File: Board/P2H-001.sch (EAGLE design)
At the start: 27 parts, among them IC1 LTC485N, IC2 74LS07N, IC3 74LS157N, IC4 LTC485N, IC5 TLC5941NT

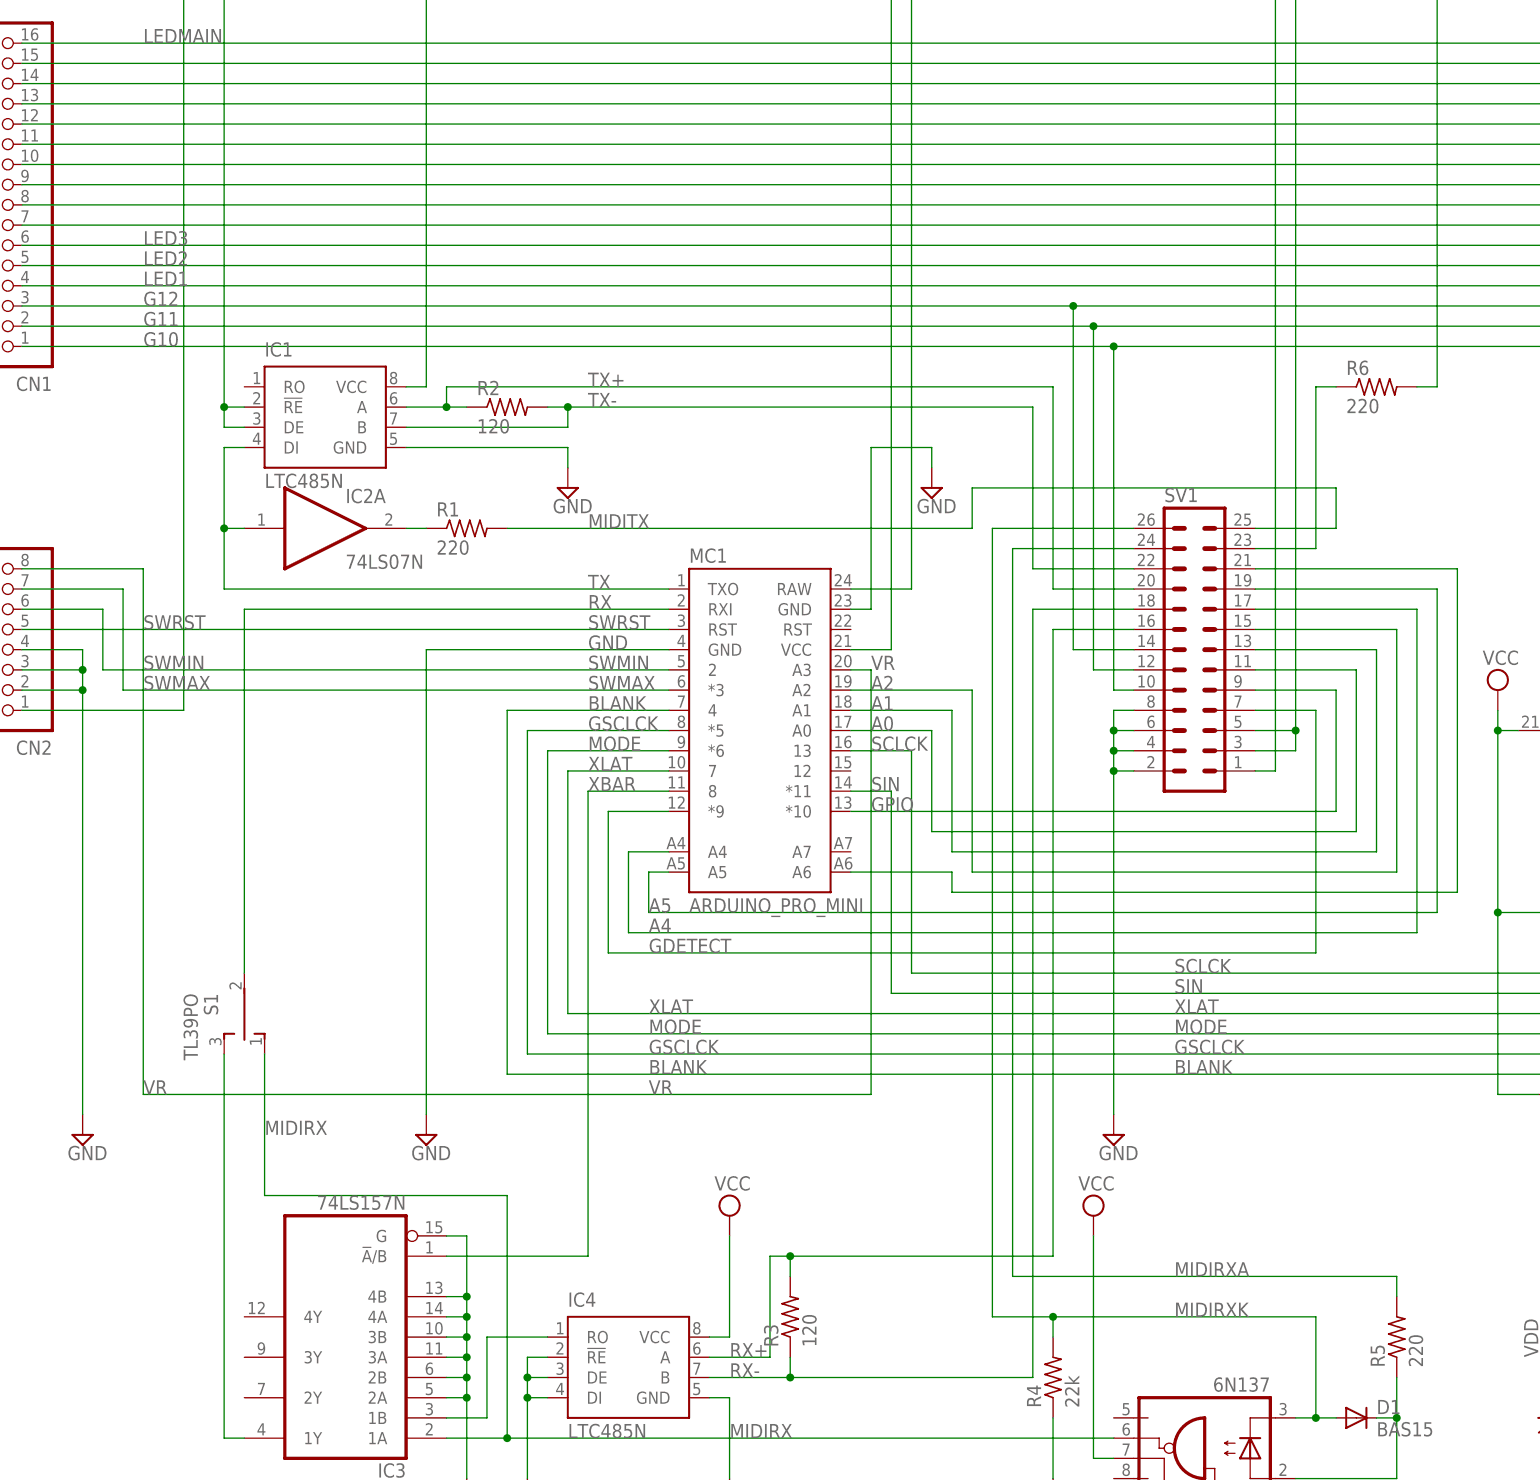
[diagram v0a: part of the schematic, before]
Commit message: Renumbered LED numbers.
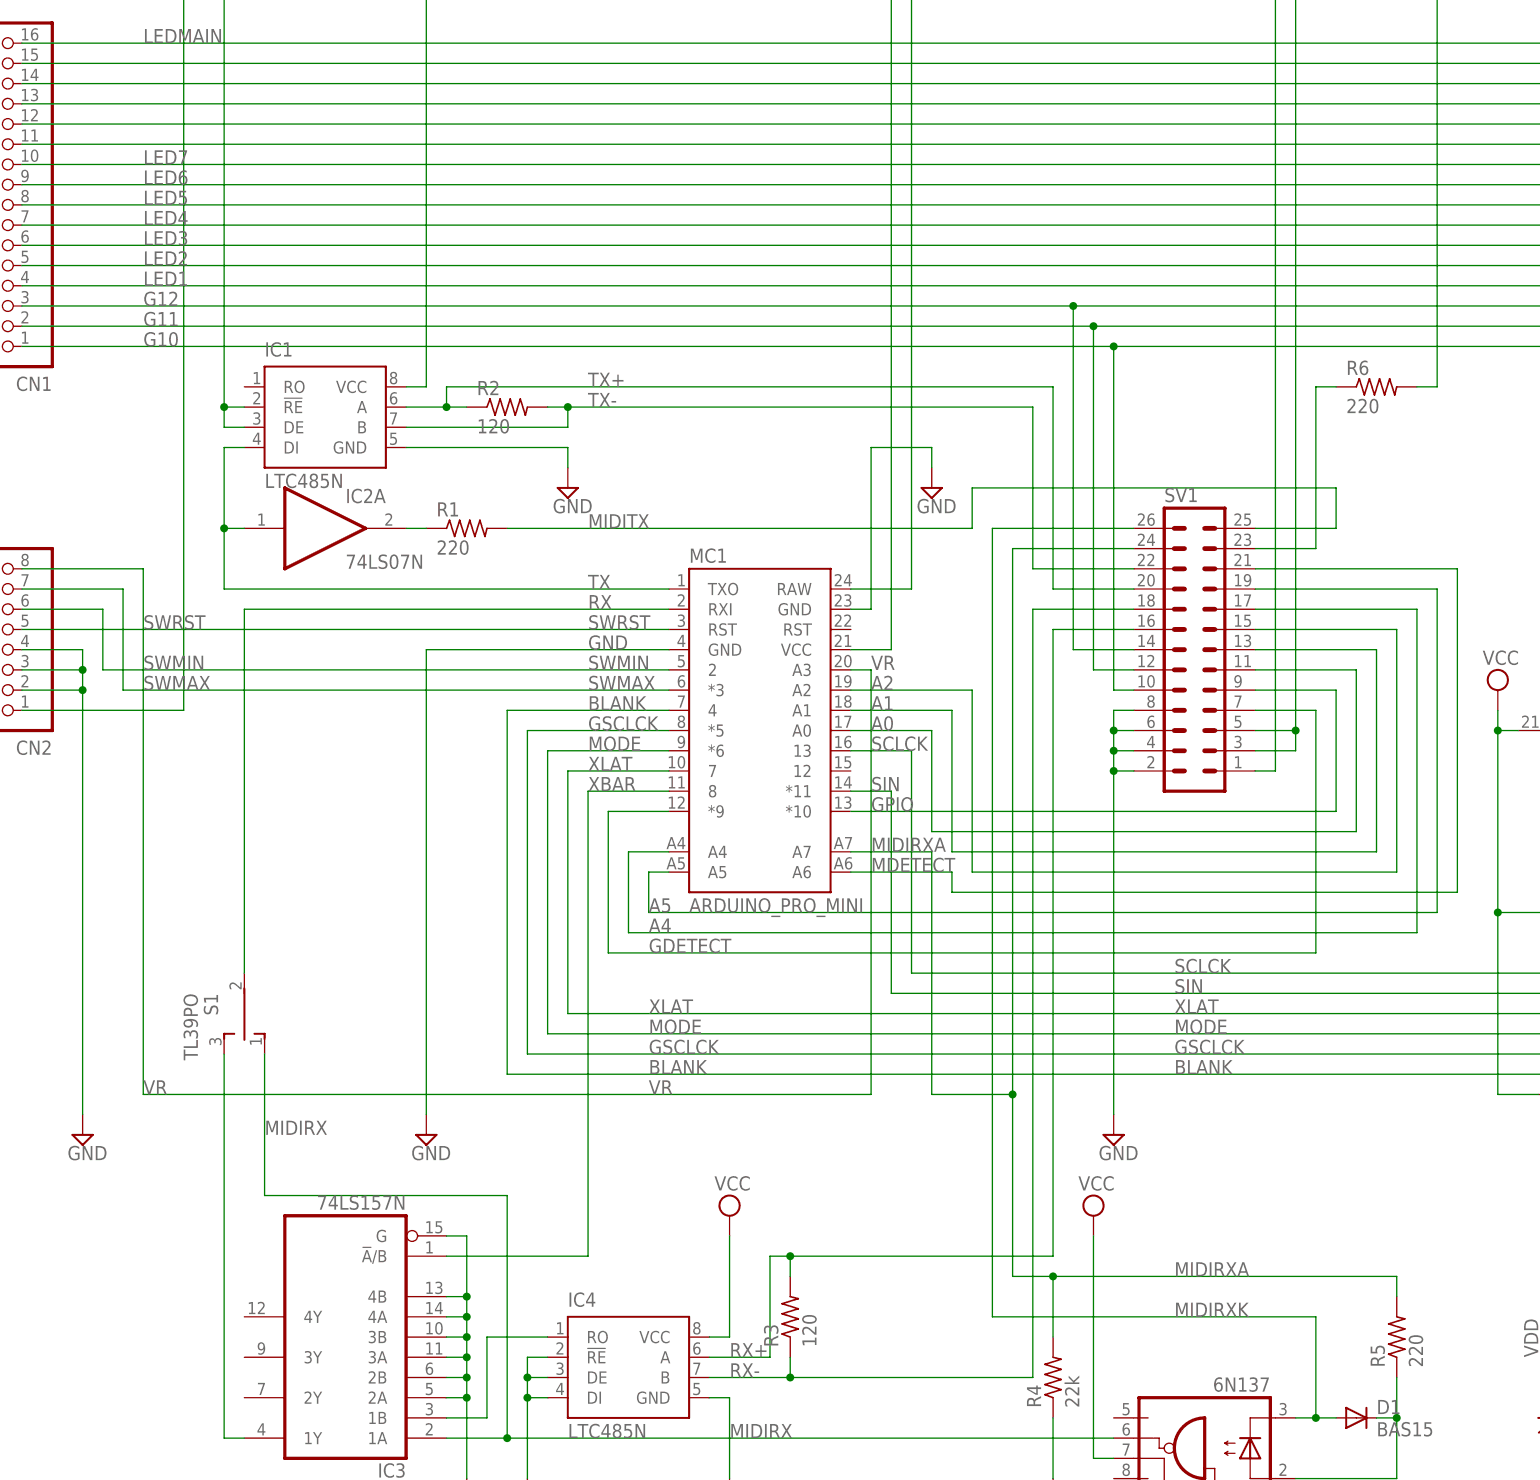
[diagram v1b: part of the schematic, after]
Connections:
- net LED3B renamed LED6
- net LED3G renamed LED5
- net LED3R renamed LED4
- net N$4 renamed MDETECT
- net N$6 renamed LED7
- net N$7 renamed LED8
- net N$8 renamed LED9
- net MIDIRXA: now also MC1.A7, R4.2
- net MIDIRXK: no longer R4.2
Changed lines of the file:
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@@
 </segment>
 </net>
-<net name="LED3R" class="0">
+<net name="LED4" class="0">
 <segment>
 <pinref part="IC5" gate="G$1" pin="OUT6"/>
@@
 <wire x1="5.08" y1="91.44" x2="215.9" y2="91.44" width="0.1524" layer="91"/>
 <pinref part="CN1" gate="G$1" pin="7"/>
-</segment>
-</net>
-<net name="LED3B" class="0">
+<label x="20.32" y="91.44" size="1.778" layer="95"/>
+</segment>
+</net>
+<net name="LED6" class="0">
 <segment>
 <pinref part="IC5" gate="G$1" pin="OUT8"/>
@@
 <wire x1="5.08" y1="96.52" x2="220.98" y2="96.52" width="0.1524" layer="91"/>
 <pinref part="CN1" gate="G$1" pin="9"/>
-</segment>
-</net>
-<net name="LED3G" class="0">
+<label x="20.32" y="96.52" size="1.778" layer="95"/>
+</segment>
+</net>
+<net name="LED5" class="0">
 <segment>
 <pinref part="IC5" gate="G$1" pin="OUT7"/>
@@
 <wire x1="5.08" y1="93.98" x2="218.44" y2="93.98" width="0.1524" layer="91"/>
 <pinref part="CN1" gate="G$1" pin="8"/>
+<label x="20.32" y="93.98" size="1.778" layer="95"/>
 </segment>
 </net>
@@
 </segment>
 </net>
-<net name="N$6" class="0">
+<net name="LED7" class="0">
 <segment>
 <pinref part="IC5" gate="G$1" pin="OUT9"/>
@@
 <wire x1="5.08" y1="99.06" x2="223.52" y2="99.06" width="0.1524" layer="91"/>
 <pinref part="CN1" gate="G$1" pin="10"/>
-</segment>
-</net>
-<net name="N$7" class="0">
+<label x="20.32" y="99.06" size="1.778" layer="95"/>
+</segment>
+</net>
+<net name="LED8" class="0">
 <segment>
 <pinref part="IC5" gate="G$1" pin="OUT10"/>
@@
 </segment>
 </net>
-<net name="N$8" class="0">
+<net name="LED9" class="0">
 <segment>
 <pinref part="IC5" gate="G$1" pin="OUT11"/>
@@
 <wire x1="167.64" y1="-58.42" x2="170.18" y2="-58.42" width="0.1524" layer="91"/>
 <wire x1="167.64" y1="-58.42" x2="167.64" y2="-45.72" width="0.1524" layer="91"/>
-<wire x1="167.64" y1="-45.72" x2="134.62" y2="-45.72" width="0.1524" layer="91"/>
+<wire x1="167.64" y1="-45.72" x2="127" y2="-45.72" width="0.1524" layer="91"/>
 <junction x="167.64" y="-58.42"/>
 <label x="149.86" y="-45.72" size="1.778" layer="95"/>
-<pinref part="R4" gate="G$1" pin="2"/>
-<wire x1="134.62" y1="-45.72" x2="134.62" y2="-48.26" width="0.1524" layer="91"/>
-<junction x="134.62" y="-45.72"/>
-<wire x1="134.62" y1="-45.72" x2="127" y2="-45.72" width="0.1524" layer="91"/>
 <wire x1="127" y1="-45.72" x2="127" y2="53.34" width="0.1524" layer="91"/>
 <pinref part="SV1" gate="1" pin="26"/>
@@
 </segment>
 </net>
-<net name="N$4" class="0">
+<net name="MDETECT" class="0">
 <segment>
 <pinref part="SV1" gate="1" pin="21"/>
@@
 <pinref part="MC1" gate="G$1" pin="A6"/>
 <wire x1="121.92" y1="10.16" x2="109.22" y2="10.16" width="0.1524" layer="91"/>
+<label x="111.76" y="10.16" size="1.778" layer="95"/>
 </segment>
 </net>
@@
 <pinref part="SV1" gate="1" pin="24"/>
 <wire x1="144.78" y1="50.8" x2="129.54" y2="50.8" width="0.1524" layer="91"/>
-<wire x1="129.54" y1="50.8" x2="129.54" y2="-40.64" width="0.1524" layer="91"/>
+<wire x1="129.54" y1="50.8" x2="129.54" y2="-17.78" width="0.1524" layer="91"/>
 <pinref part="R5" gate="G$1" pin="2"/>
-<wire x1="129.54" y1="-40.64" x2="177.8" y2="-40.64" width="0.1524" layer="91"/>
+<wire x1="129.54" y1="-17.78" x2="129.54" y2="-40.64" width="0.1524" layer="91"/>
+<wire x1="129.54" y1="-40.64" x2="134.62" y2="-40.64" width="0.1524" layer="91"/>
+<wire x1="134.62" y1="-40.64" x2="177.8" y2="-40.64" width="0.1524" layer="91"/>
 <wire x1="177.8" y1="-40.64" x2="177.8" y2="-43.18" width="0.1524" layer="91"/>
 <label x="149.86" y="-40.64" size="1.778" layer="95"/>
-</segment>
-</net>
+<pinref part="MC1" gate="G$1" pin="A7"/>
+<wire x1="109.22" y1="12.7" x2="119.38" y2="12.7" width="0.1524" layer="91"/>
+<wire x1="119.38" y1="12.7" x2="119.38" y2="-17.78" width="0.1524" layer="91"/>
+<wire x1="119.38" y1="-17.78" x2="129.54" y2="-17.78" width="0.1524" layer="91"/>
+<junction x="129.54" y="-17.78"/>
+<label x="111.76" y="12.7" size="1.778" layer="95"/>
+<pinref part="R4" gate="G$1" pin="2"/>
+<wire x1="134.62" y1="-40.64" x2="134.62" y2="-48.26" width="0.1524" layer="91"/>
+<junction x="134.62" y="-40.64"/>
+</segment>
+</net>

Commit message: Still updating.
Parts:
- removed SV2: (no value), con-ml:ML10
- added JP1: (no value), pinhead:PINHD-2X5
- added U$1: MAX7219DIP, SparkFun-DigitalIC:MAX7219DIP
- IC5: value TLC5941NT -> 4051N; device adafruit:TLC5941NT -> 40xx:4051N
- R7: value 4.7k -> (none)
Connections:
- removed net A4: MC1.A4, SV1.17
- removed net A5: MC1.A5, SV1.19
- removed net G10: CN1.1, IC5.OUT0, SV1.10
- removed net G11: CN1.2, IC5.OUT1, SV1.12
- removed net G12: CN1.3, IC5.OUT2, SV1.14
- removed net GDETECT: MC1.*9, SV1.7
- removed net GPIO: MC1.*10, SV1.9
- removed net GSCLCK: IC5.GSCLK, MC1.*5, SV2.7
- removed net LED1: CN1.4, IC5.OUT3
- removed net LED2: CN1.5, IC5.OUT4
- removed net LED3: CN1.6, IC5.OUT5
- removed net LED4: CN1.7, IC5.OUT6
- removed net LED5: CN1.8, IC5.OUT7
- removed net LED6: CN1.9, IC5.OUT8
- removed net LED7: CN1.10, IC5.OUT9
- removed net LED8: CN1.11, IC5.OUT10
- removed net LED9: CN1.12, IC5.OUT11
- removed net LEDMAIN: CN1.16, IC5.OUT15
- removed net MDETECT: MC1.A6, SV1.21
- removed net MODE: IC5.MODE, MC1.*6, SV2.8
- removed net N$10: IC5.SOUT, SV2.3
- removed net N$20: R6.1, SV1.23
- removed net N$37: IC5.IREF, R7.2
- removed net SIN: IC5.SIN, MC1.*11
- removed net VR: CN2.8, MC1.A3
- removed net XLAT: IC5.XLAT, MC1.7, SV2.6
- new net ADETECT: IC5A.X, MC1.A3
- new net DOUT: JP1.4, U$1.DOUT
- new net GSELECT: MC1.*10, SV1.15
- new net LA0: CN1.9, U$1.SEGDP
- new net LK0: CN1.1, U$1.DIG0
- new net LOAD: JP1.6, MC1.7, U$1.LOAD
- new net MOSI: JP1.3, MC1.*11, U$1.DIN
- new net N$12: R6.1, SV1.20
- new net N$18: CN1.3, U$1.DIG2
- new net N$19: CN1.4, U$1.DIG3
- new net N$21: R7.1, U$1.ISET
- new net N$22: CN1.2, U$1.DIG1
- new net N$25: CN1.6, U$1.DIG5
- new net N$26: CN1.7, U$1.DIG6
- new net N$27: CN1.8, U$1.DIG7
- new net N$29: CN1.10, U$1.SEGA
- new net N$30: CN1.11, U$1.SEGB
- new net N$31: CN1.12, U$1.SEGC
- new net N$32: CN1.13, U$1.SEGD
- new net N$33: CN1.14, U$1.SEGE
- new net N$34: CN1.15, U$1.SEGF
- new net N$35: CN1.16, U$1.SEGG
- new net N$6: IC5A.X3, SV1.14
- new net OUT1: MC1.*5, SV1.17
- new net OUT2: MC1.*6, SV1.19
- new net OUT3: MC1.*9, SV1.21
- new net SDA: MC1.A4, SV1.9
- new net SDL: MC1.A5, SV1.11
- new net SELECT0: IC5A.A, MC1.A6
- new net SELECT1: IC5A.B, MC1.A7
- new net VDETECT: CN2.8, IC5A.X0
- net A0: now also SV1.3; no longer SV1.11
- net A1: now also SV1.5; no longer SV1.13
- net A2: now also SV1.7; no longer SV1.15
- net BLANK: now also JP1.7, MC1.8; no longer IC5.BLANK, MC1.4, SV2.5
- net GND: now also IC5A.C, IC5A.INH, JP1.2, U$1.GND, U$1.GND2; no longer IC5.GND, SV2.10, SV2.2
- net MIDIRXA: now also SV1.16; no longer MC1.A7, R4.2, SV1.24
- net MIDIRXK: now also SV1.18; no longer SV1.26
- net MIDITX: now also SV1.22; no longer SV1.25
- net N$24: now also CN1.5, U$1.DIG4; no longer CN1.15, IC5.OUT14
- net N$3: now also IC5A.X1, SV1.13; no longer CN1.13, IC5.OUT12
- net N$5: now also IC5A.X2, R4.2, SV1.12; no longer CN1.14, IC5.OUT13
- net RX+: now also R3.1, SV1.24; no longer R3.2, SV1.16
- net RX-: now also R3.2, SV1.26; no longer R3.1, SV1.18
- net SCLCK: now also JP1.5, U$1.CLK; no longer IC5.SCLK, SV2.4
- net SWMAX: now also JP1.9
- net SWMIN: now also JP1.8
- net TX+: now also SV1.23; no longer SV1.20
- net TX-: now also SV1.25; no longer SV1.22
- net VCC: now also JP1.1, R7.2, U$1.VCC; no longer IC5.TEST, IC5.VCC, R7.1, SV2.1
- net VDD: now also JP1.10, SV1.10; no longer SV1.3, SV1.5, SV2.9
- net XBAR: now also MC1.4; no longer MC1.8
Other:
- note added: "Pineapple II Hydrogen 0.4.0 Copyright 2015 by Pineapple.cc"
- note removed: "Pineapple II Hydrogen 0.3.0 Copyright 2015 by Pineapple.cc"
- moved on the sheet: C1, C2, C3, C4, C5, C6, C7, CN1, D1, IC1, IC2A, IC2B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

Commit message: Autorouted.
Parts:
- IC1: value LTC485N -> 74LS157N; device linear-technology:LTC485N -> 74xx-us:74LS157N
- IC2: value 74LS07N -> LTC485N; device 74xx-us:74LS07N -> linear-technology:LTC485N
- IC3: value 74LS157N -> 4051N; device 74xx-us:74LS157N -> 40xx:4051N
- IC4: value LTC485N -> 74LS07N; device linear-technology:LTC485N -> 74xx-us:74LS07N
- IC5: value 4051N -> LTC485N; device 40xx:4051N -> linear-technology:LTC485N
- R1, R6: value 220 -> 120
- R2: value 120 -> 220
- R3: value 120 -> 22k
- R4: value 22k -> 220
- renumbered U$1 to MC2
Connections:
- net ADETECT: now also IC3A.X; no longer IC5A.X
- net GND: now also IC1A.2A, IC1A.2B, IC1A.3A, IC1A.3B, IC1A.4A, IC1A.4B, IC1A.G, IC2.!RE, IC2.DE, IC2.DI, IC2.GND, IC3A.C, IC3A.INH, IC4B.I, IC4C.I, IC4D.I, IC4E.I, IC4F.I, IC5.GND, R3.1; no longer IC1.GND, IC2B.I, IC2C.I, IC2D.I, IC2E.I, IC2F.I, IC3A.2A, IC3A.2B, IC3A.3A, IC3A.3B, IC3A.4A, IC3A.4B, IC3A.G, IC4.!RE, IC4.DE, IC4.DI, IC4.GND, IC5A.C, IC5A.INH, R4.1
- net HSRX: now also IC1A.1B, IC2.RO; no longer IC3A.1B, IC4.RO
- net MIDIRX: now also IC1A.1A; no longer IC3A.1A
- net MIDIRXA: now also R2.2; no longer R5.2
- net MIDITX: now also R5.2; no longer R1.2
- net N$1: now also IC1A.1Y; no longer IC3A.1Y
- net N$12: now also R4.1; no longer R6.1
- net N$13: now also R2.1; no longer R5.1
- net N$2: now also IC4A.O, R5.1; no longer IC2A.O, R1.1
- net N$3: now also IC3A.X1; no longer IC5A.X1
- net N$5: now also IC3A.X2, R3.2; no longer IC5A.X2, R4.2
- net N$6: now also IC3A.X3; no longer IC5A.X3
- net RX+: now also IC2.A, R1.1; no longer IC4.A, R3.1
- net RX-: now also IC2.B, R1.2; no longer IC4.B, R3.2
- net SELECT0: now also IC3A.A; no longer IC5A.A
- net SELECT1: now also IC3A.B; no longer IC5A.B
- net TX: now also IC4A.I, IC5.DI; no longer IC1.DI, IC2A.I
- net TX+: now also IC5.A, R6.1; no longer IC1.A, R2.1
- net TX-: now also IC5.B, R6.2; no longer IC1.B, R2.2
- net VCC: now also IC2.VCC, IC5.!RE, IC5.DE, IC5.VCC, R4.2; no longer IC1.!RE, IC1.DE, IC1.VCC, IC4.VCC, R6.2
- net VDETECT: now also IC3A.X0; no longer IC5A.X0
- net XBAR: now also IC1A.!A!/B; no longer IC3A.!A!/B
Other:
- moved on the sheet: C1, C2, C3, C4, C5, C6, C7, R1, R2, R3, R4, R5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

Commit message: Autorouted 2.
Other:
- moved on the sheet: C1, C2, C3, C4, C5, C6, C7, CN1, CN2, D1, IC2, IC4A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
